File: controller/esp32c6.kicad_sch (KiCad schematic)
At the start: 13 parts, among them J10 Conn_ARM_JTAG_SWD_10, SW1 Boot, SW2 Reset, U6 ESP32-C6-WROOM-1

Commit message: Controller - some more changes
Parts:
- added D23, D24, D25: CLMUD-FKC-CHJNPM569ABB845343, Library:LED_Cree-PLCC4_1.5x1.5mm, symbol Device:LED_ARGB
- added R49, R50, R57, R58, R59, R60, R64, R65, R66: ?, Resistor_SMD:R_0402_1005Metric, symbol Device:R_Small
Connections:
- net +3V3: now also D23.1 (A), D24.1 (A), D25.1 (A)
- net RX: now also U6.24 (U0RXD/GPIO17); no longer U6.20 (GPIO22)
- net TX: now also U6.25 (U0TXD/GPIO16); no longer U6.21 (GPIO23)
- net IO10: now reaches U6.11 (GPIO10)
- net IO10: now also R49.1
- net IO11: now reaches U6.12 (GPIO11)
- net IO11: now also R50.1
- net IO18: now reaches U6.16 (GPIO18)
- net IO18: now also R58.1
- net IO19: now reaches U6.17 (GPIO19)
- net IO19: now also R59.1
- net IO15: now reaches U6.23 (GPIO15)
- net IO15: now also R57.1
- net IO3: now reaches U6.26 (GPIO3/ADC1_CH3)
- net IO3: now also R66.1
- net IO2: now reaches U6.27 (GPIO2/ADC1_CH2)
- net IO2: now also R65.1
- net IO0: now reaches U6.8 (GPIO0/ADC1_CH0/XTAL_32K_P)
- net IO0: now also R60.1
- net IO1: now reaches U6.9 (GPIO1/ADC1_CH1/XTAL_32K_N)
- net IO1: now also R64.1
- new net: D25.4 (BK), R66.2
- new net: D25.3 (GK), R65.2
- new net: D23.4 (BK), R57.2
- new net: D24.4 (BK), R60.2
- new net: D25.2 (RK), R64.2
- new net: D24.3 (GK), R59.2
- new net: D24.2 (RK), R58.2
- new net: D23.3 (GK), R50.2
- new net: D23.2 (RK), R49.2

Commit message: Controller - more changes
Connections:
- net B_BOOT: now reaches R7.2, SW1.1, U6.15 (GPIO9)
- net R: now reaches R10.2, U6.10 (GPIO8)
- net G: now reaches U6.20 (GPIO22)
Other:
- moved on the sheet: R10, R7, SW1
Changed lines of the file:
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@@
 	)
 	(junction
+		(at 92.71 88.9)
+		(diameter 0)
+		(color 0 0 0 0)
+	)
+	(junction
 		(at 146.05 60.96)
 		(diameter 0)
@@
 	)
 	(junction
+		(at 95.25 93.98)
+		(diameter 0)
+		(color 0 0 0 0)
+	)
+	(junction
+		(at 90.17 96.52)
+		(diameter 0)
+		(color 0 0 0 0)
+	)
+	(junction
 		(at 151.13 60.96)
 		(diameter 0)
@@
 		(color 0 0 0 0)
 	)
-	(junction
-		(at 93.98 88.9)
-		(diameter 0)
-		(color 0 0 0 0)
+	(wire
+		(pts
+			(xy 80.01 93.98) (xy 80.01 95.25)
+		)
+		(stroke
+			(width 0)
+			(type default)
+		)
 	)
 	(wire
@@
 	(wire
 		(pts
+			(xy 91.44 96.52) (xy 91.44 100.33)
+		)
+		(stroke
+			(width 0)
+			(type default)
+		)
+	)
+	(wire
+		(pts
 			(xy 170.18 93.98) (xy 171.45 93.98)
 		)
@@
 	(wire
 		(pts
+			(xy 90.17 96.52) (xy 91.44 96.52)
+		)
+		(stroke
+			(width 0)
+			(type default)
+		)
+	)
+	(wire
+		(pts
 			(xy 87.63 81.28) (xy 100.33 81.28)
 		)
@@
 	(wire
 		(pts
-			(xy 156.21 101.6) (xy 162.56 101.6)
+			(xy 95.25 93.98) (xy 100.33 93.98)
 		)
 		(stroke
@@
 	(wire
 		(pts
-			(xy 171.45 66.04) (xy 171.45 67.31)
+			(xy 156.21 101.6) (xy 162.56 101.6)
 		)
 		(stroke
@@
 	(wire
 		(pts
-			(xy 93.98 88.9) (xy 96.52 88.9)
+			(xy 171.45 66.04) (xy 171.45 67.31)
 		)
 		(stroke
@@
 	(wire
 		(pts
+			(xy 92.71 88.9) (xy 90.17 88.9)
+		)
+		(stroke
+			(width 0)
+			(type default)
+		)
+	)
+	(wire
+		(pts
 			(xy 90.17 111.76) (xy 100.33 111.76)
 		)
@@
 	(wire
 		(pts
-			(xy 93.98 88.9) (xy 91.44 88.9)
+			(xy 92.71 88.9) (xy 95.25 88.9)
+		)
+		(stroke
+			(width 0)
+			(type default)
+		)
+	)
+	(wire
+		(pts
+			(xy 77.47 93.98) (xy 80.01 93.98)
 		)
 		(stroke
@@
 	(wire
 		(pts
-			(xy 90.17 96.52) (xy 91.44 96.52)
+			(xy 90.17 100.33) (xy 91.44 100.33)
 		)
 		(stroke
@@
 	(wire
 		(pts
-			(xy 96.52 93.98) (xy 100.33 93.98)
-		)
-		(stroke
-			(width 0)
-			(type default)
-		)
-	)
-	(wire
-		(pts
 			(xy 151.13 60.96) (xy 156.21 60.96)
 		)
@@
 	(wire
 		(pts
-			(xy 91.44 93.98) (xy 91.44 96.52)
+			(xy 90.17 93.98) (xy 90.17 96.52)
 		)
 		(stroke
@@
 	(wire
 		(pts
+			(xy 93.98 95.25) (xy 93.98 93.98)
+		)
+		(stroke
+			(width 0)
+			(type default)
+		)
+	)
+	(wire
+		(pts
 			(xy 156.21 96.52) (xy 160.02 96.52)
 		)
@@
 	(wire
 		(pts
-			(xy 80.01 96.52) (xy 80.01 101.6)
+			(xy 80.01 100.33) (xy 80.01 105.41)
+		)
+		(stroke
+			(width 0)
+			(type default)
+		)
+	)
+	(wire
+		(pts
+			(xy 93.98 93.98) (xy 95.25 93.98)
+		)
+		(stroke
+			(width 0)
+			(type default)
+		)
+	)
+	(wire
+		(pts
+			(xy 77.47 96.52) (xy 90.17 96.52)
 		)
 		(stroke
@@
 		)
 	)
+	(wire
+		(pts
+			(xy 80.01 95.25) (xy 93.98 95.25)
+		)
+		(stroke
+			(width 0)
+			(type default)
+		)
+	)
 	(label "IO19"
 		(at 133.35 43.18 270)
@@
 		)
 	)
+	(hierarchical_label "B_BOOT"
+		(shape bidirectional)
+		(at 77.47 96.52 180)
+		(fields_autoplaced yes)
+		(effects
+			(font
+				(size 1.27 1.27)
+			)
+			(justify right)
+		)
+	)
 	(hierarchical_label "USB_D+"
 		(shape bidirectional)
@@
 		)
 	)
+	(hierarchical_label "G"
+		(shape input)
+		(at 100.33 116.84 180)
+		(fields_autoplaced yes)
+		(effects
+			(font
+				(size 1.27 1.27)
+			)
+			(justify right)
+		)
+	)
 	(hierarchical_label "GPIO20"
 		(shape bidirectional)
@@
 		)
 	)
+	(hierarchical_label "R"
+		(shape output)
+		(at 77.47 93.98 180)
+		(fields_autoplaced yes)
+		(effects
+			(font
+				(size 1.27 1.27)
+			)
+			(justify right)
+		)
+	)
 	(hierarchical_label "USB_D-"
 		(shape bidirectional)
@@
 	(symbol
 		(lib_id "Device:R_Small")
-		(at 91.44 91.44 0)
+		(at 90.17 91.44 0)
 		(unit 1)
 		(exclude_from_sim no)
@@
 		(dnp no)
 		(property "Reference" "R7"
-			(at 89.408 98.044 0)
+			(at 88.138 98.044 0)
 			(effects
 				(font
@@
 		)
 		(property "Value" "10k"
-			(at 91.44 93.218 90)
+			(at 90.17 93.218 90)
 			(effects
 				(font
@@
 		)
 		(property "Footprint" "Resistor_SMD:R_0603_1608Metric"
-			(at 91.44 91.44 0)
+			(at 90.17 91.44 0)
 			(effects
 				(font
@@
 		)
 		(property "Datasheet" "~"
-			(at 91.44 91.44 0)
+			(at 90.17 91.44 0)
 			(effects
 				(font
@@
 		)
 		(property "Description" "Resistor, small symbol"
-			(at 91.44 91.44 0)
+			(at 90.17 91.44 0)
 			(effects
 				(font
@@
 	(symbol
 		(lib_id "power:Earth")
-		(at 80.01 101.6 0)
+		(at 80.01 105.41 0)
 		(mirror y)
 		(unit 1)
@@
 		(fields_autoplaced yes)
 		(property "Reference" "#PWR043"
-			(at 80.01 107.95 0)
+			(at 80.01 111.76 0)
 			(effects
 				(font
@@
 		)
 		(property "Value" "Earth"
-			(at 80.01 106.68 0)
+			(at 80.01 110.49 0)
 			(effects
 				(font
@@
 		)
 		(property "Footprint" ""
-			(at 80.01 101.6 0)
+			(at 80.01 105.41 0)
 			(effects
 				(font
@@
 		)
 		(property "Datasheet" "~"
-			(at 80.01 101.6 0)
+			(at 80.01 105.41 0)
 			(effects
 				(font
@@
 		)
 		(property "Description" "Power symbol creates a global label with name \"Earth\""
-			(at 80.01 101.6 0)
+			(at 80.01 105.41 0)
 			(effects
 				(font
@@
 	(symbol
 		(lib_id "power:+3V3")
-		(at 93.98 88.9 0)
+		(at 92.71 88.9 0)
 		(unit 1)
 		(exclude_from_sim no)
@@
 		(fields_autoplaced yes)
 		(property "Reference" "#PWR044"
-			(at 93.98 92.71 0)
+			(at 92.71 92.71 0)
 			(effects
 				(font
@@
 		)
 		(property "Value" "+3V3"
-			(at 93.98 85.09 0)
+			(at 92.71 85.09 0)
 			(effects
 				(font
@@
 		)
 		(property "Footprint" ""
-			(at 93.98 88.9 0)
+			(at 92.71 88.9 0)
 			(effects
 				(font
@@
 		)
 		(property "Datasheet" ""
-			(at 93.98 88.9 0)
+			(at 92.71 88.9 0)
 			(effects
 				(font
@@
 		)
 		(property "Description" "Power symbol creates a global label with name \"+3V3\""
-			(at 93.98 88.9 0)
+			(at 92.71 88.9 0)
 			(effects
 				(font
@@
 	(symbol
 		(lib_id "Device:R_Small")
-		(at 96.52 91.44 0)
+		(at 95.25 91.44 0)
 		(unit 1)
 		(exclude_from_sim no)
@@
 		(dnp no)
 		(property "Reference" "R10"
-			(at 94.742 95.25 0)
+			(at 96.266 90.17 0)
 			(effects
 				(font
@@
 		)
 		(property "Value" "10k"
-			(at 96.52 93.218 90)
+			(at 95.25 93.218 90)
 			(effects
 				(font
@@
 		)
 		(property "Footprint" "Resistor_SMD:R_0603_1608Metric"
-			(at 96.52 91.44 0)
+			(at 95.25 91.44 0)
 			(effects
 				(font
@@
 		)
 		(property "Datasheet" "~"
-			(at 96.52 91.44 0)
+			(at 95.25 91.44 0)
 			(effects
 				(font
@@
 		)
 		(property "Description" "Resistor, small symbol"
-			(at 96.52 91.44 0)
+			(at 95.25 91.44 0)
 			(effects
 				(font
@@
 	(symbol
 		(lib_id "Switch:SW_Push")
-		(at 85.09 96.52 0)
+		(at 85.09 100.33 0)
 		(mirror y)
 		(unit 1)
@@
 		(on_board yes)
 		(dnp no)
-		(fields_autoplaced yes)
 		(property "Reference" "SW1"
-			(at 85.09 88.9 0)
+			(at 85.09 101.854 0)
 			(effects
 				(font
@@
 		)
 		(property "Value" "Boot"
-			(at 85.09 91.44 0)
+			(at 85.09 104.394 0)
 			(effects
 				(font
@@
 		)
 		(property "Footprint" ""
-			(at 85.09 91.44 0)
+			(at 85.09 95.25 0)
 			(effects
 				(font
@@
 		)
 		(property "Datasheet" "~"
-			(at 85.09 91.44 0)
+			(at 85.09 95.25 0)
 			(effects
 				(font
@@
 		)
 		(property "Description" "Push button switch, generic, two pins"
-			(at 85.09 96.52 0)
+			(at 85.09 100.33 0)
 			(effects
 				(font

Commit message: Controller - Even more pins
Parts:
- J10: footprint (none) -> Connector_PinHeader_1.27mm:PinHeader_2x05_P1.27mm_Vertical_SMD
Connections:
- net +3V3: now also J10.1 (VTref)
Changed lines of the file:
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@@
+	)
+	(symbol
+		(lib_id "power:+3V3")
+		(at 184.15 86.36 0)
+		(unit 1)
+		(exclude_from_sim no)
+		(in_bom yes)
+		(on_board yes)
+		(dnp no)
+		(fields_autoplaced yes)
+		(property "Reference" "#PWR0143"
+			(at 184.15 90.17 0)
+			(effects
+				(font
+					(size 1.27 1.27)
+				)
+				(hide yes)
+			)
+		)
+		(property "Value" "+3V3"
+			(at 184.15 82.55 0)
+			(effects
+				(font
+					(size 1.27 1.27)
+				)
+			)
+		)
+		(property "Footprint" ""
+			(at 184.15 86.36 0)
+			(effects
+				(font
+					(size 1.27 1.27)
+				)
+				(hide yes)
+			)
+		)
+		(property "Datasheet" ""
+			(at 184.15 86.36 0)
+			(effects
+				(font
+					(size 1.27 1.27)
+				)
+				(hide yes)
+			)
+		)
+		(property "Description" "Power symbol creates a global label with name \"+3V3\""
+			(at 184.15 86.36 0)
+			(effects
+				(font
+					(size 1.27 1.27)
+				)
+				(hide yes)
+			)
+		)
+		(pin "1"
+		)
+		(instances
+			(project "controller"
+				(path "/5b092a03-7e3e-4df1-ad91-2ac0e362f857/d740d1c6-5e66-443f-883c-6d6068be0c77"
+					(reference "#PWR0143")
+					(unit 1)
+				)
+			)
+		)
 	)
 	(symbol
@@
 			)
 		)
-		(property "Footprint" ""
+		(property "Footprint" "Connector_PinHeader_1.27mm:PinHeader_2x05_P1.27mm_Vertical_SMD"
 			(at 184.15 101.6 0)
 			(effects

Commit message: Add new leds
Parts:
- removed D23, D24, D25: CLMUD-FKC-CHJNPM569ABB845343, Library:LED_Cree-PLCC4_1.5x1.5mm, symbol Device:LED_ARGB
- removed R49, R50, R57, R58, R59, R60, R64, R65, R66: ?, Resistor_SMD:R_0402_1005Metric, symbol Device:R_Small
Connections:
- net G renamed LED_CH2
- net IO0: no longer names the net of U6.8 (GPIO0/ADC1_CH0/XTAL_32K_P)
- net IO1: no longer names the net of U6.9 (GPIO1/ADC1_CH1/XTAL_32K_N)
- net IO10: no longer names the net of U6.11 (GPIO10)
- net IO11: no longer names the net of U6.12 (GPIO11)
- net IO15: no longer names the net of U6.23 (GPIO15)
- net IO18: no longer names the net of U6.16 (GPIO18)
- net IO19: no longer names the net of U6.17 (GPIO19)
- net IO2: no longer names the net of U6.27 (GPIO2/ADC1_CH2)
- net IO3: no longer names the net of U6.26 (GPIO3/ADC1_CH3)
- net R renamed LED_CH1

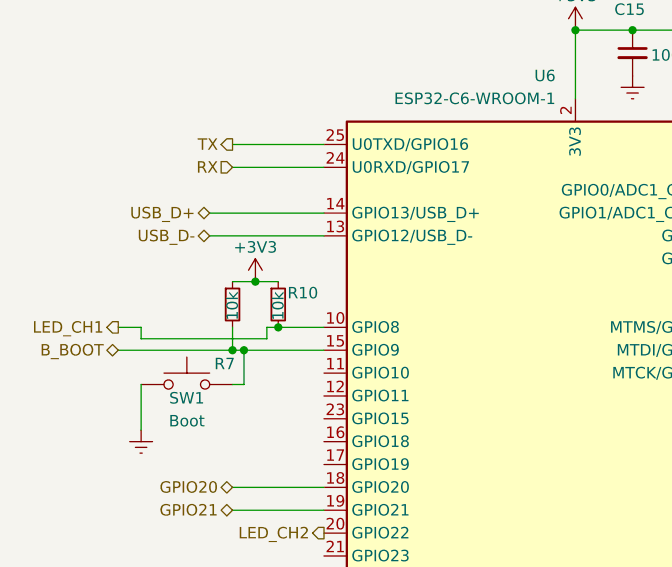
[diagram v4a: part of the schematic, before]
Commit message: Controller - Most things routed
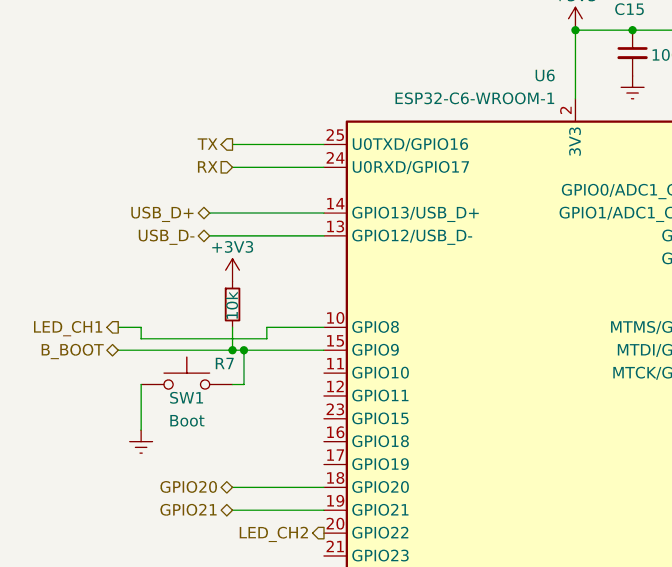
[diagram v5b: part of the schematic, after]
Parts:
- removed R10: 10k, Resistor_SMD:R_0603_1608Metric, symbol Device:R_Small
- R11: footprint Resistor_SMD:R_0603_1608Metric -> Resistor_SMD:R_0402_1005Metric
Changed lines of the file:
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@@
-	)
-	(junction
-		(at 92.71 88.9)
-		(diameter 0)
-		(color 0 0 0 0)
 	)
 	(junction
@@
 	)
 	(junction
-		(at 95.25 93.98)
-		(diameter 0)
-		(color 0 0 0 0)
-	)
-	(junction
 		(at 90.17 96.52)
 		(diameter 0)
@@
 	(wire
 		(pts
-			(xy 95.25 93.98) (xy 100.33 93.98)
+			(xy 93.98 93.98) (xy 100.33 93.98)
 		)
 		(stroke
@@
 	(wire
 		(pts
-			(xy 92.71 88.9) (xy 90.17 88.9)
-		)
-		(stroke
-			(width 0)
-			(type default)
-		)
-	)
-	(wire
-		(pts
 			(xy 90.17 111.76) (xy 100.33 111.76)
 		)
@@
 	(wire
 		(pts
-			(xy 92.71 88.9) (xy 95.25 88.9)
-		)
-		(stroke
-			(width 0)
-			(type default)
-		)
-	)
-	(wire
-		(pts
 			(xy 77.47 93.98) (xy 80.01 93.98)
 		)
@@
 		(pts
 			(xy 80.01 100.33) (xy 80.01 105.41)
-		)
-		(stroke
-			(width 0)
-			(type default)
-		)
-	)
-	(wire
-		(pts
-			(xy 93.98 93.98) (xy 95.25 93.98)
 		)
 		(stroke
@@
 	(symbol
 		(lib_id "power:+3V3")
-		(at 92.71 88.9 0)
+		(at 90.17 88.9 0)
 		(unit 1)
 		(exclude_from_sim no)
@@
 		(fields_autoplaced yes)
 		(property "Reference" "#PWR044"
-			(at 92.71 92.71 0)
+			(at 90.17 92.71 0)
 			(effects
 				(font
@@
 		)
 		(property "Value" "+3V3"
-			(at 92.71 85.09 0)
+			(at 90.17 85.09 0)
 			(effects
 				(font
@@
 		)
 		(property "Footprint" ""
-			(at 92.71 88.9 0)
+			(at 90.17 88.9 0)
 			(effects
 				(font
@@
 		)
 		(property "Datasheet" ""
-			(at 92.71 88.9 0)
+			(at 90.17 88.9 0)
 			(effects
 				(font
@@
 		)
 		(property "Description" "Power symbol creates a global label with name \"+3V3\""
-			(at 92.71 88.9 0)
+			(at 90.17 88.9 0)
 			(effects
 				(font
@@
 	)
 	(symbol
-		(lib_id "Device:R_Small")
-		(at 95.25 91.44 0)
-		(unit 1)
-		(exclude_from_sim no)
-		(in_bom yes)
-		(on_board yes)
-		(dnp no)
-		(property "Reference" "R10"
-			(at 96.266 90.17 0)
-			(effects
-				(font
-					(size 1.27 1.27)
-				)
-				(justify left)
-			)
-		)
-		(property "Value" "10k"
-			(at 95.25 93.218 90)
-			(effects
-				(font
-					(size 1.27 1.27)
-				)
-				(justify left)
-			)
-		)
-		(property "Footprint" "Resistor_SMD:R_0603_1608Metric"
-			(at 95.25 91.44 0)
-			(effects
-				(font
-					(size 1.27 1.27)
-				)
-				(hide yes)
-			)
-		)
-		(property "Datasheet" "~"
-			(at 95.25 91.44 0)
-			(effects
-				(font
-					(size 1.27 1.27)
-				)
-				(hide yes)
-			)
-		)
-		(property "Description" "Resistor, small symbol"
-			(at 95.25 91.44 0)
-			(effects
-				(font
-					(size 1.27 1.27)
-				)
-				(hide yes)
-			)
-		)
-		(pin "1"
-		)
-		(pin "2"
-		)
-		(instances
-			(project "controller"
-				(path "/5b092a03-7e3e-4df1-ad91-2ac0e362f857/d740d1c6-5e66-443f-883c-6d6068be0c77"
-					(reference "R10")
-					(unit 1)
-				)
-			)
-		)
-	)
-	(symbol
 		(lib_id "power:Earth")
 		(at 146.05 66.04 0)
@@
 			)
 		)
-		(property "Footprint" "Resistor_SMD:R_0603_1608Metric"
+		(property "Footprint" "Resistor_SMD:R_0402_1005Metric"
 			(at 171.45 69.85 0)
 			(effects

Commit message: Controller - Fix all DRC errors and some warnings
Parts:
- SW1, SW2: footprint (none) -> Button_Switch_SMD:SW_SPST_B3U-1000P
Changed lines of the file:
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@@
 			)
 		)
-		(property "Footprint" ""
+		(property "Footprint" "Button_Switch_SMD:SW_SPST_B3U-1000P"
 			(at 193.04 68.58 0)
 			(effects
@@
 			)
 		)
-		(property "Footprint" ""
+		(property "Footprint" "Button_Switch_SMD:SW_SPST_B3U-1000P"
 			(at 85.09 95.25 0)
 			(effects

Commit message: controller - Update BOM - WIP
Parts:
- C15, C20: value 100nF -> 100nF 9V
- C16, C17, C18: value 10uF -> 10uF 9V
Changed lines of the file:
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@@
 			)
 		)
-		(property "Value" "10uF"
+		(property "Value" "10uF 9V"
 			(at 148.336 69.85 0)
 			(effects
@@
 		)
 		(property "Description" "Unpolarized capacitor, small symbol"
+			(at 151.13 63.5 0)
+			(effects
+				(font
+					(size 1.27 1.27)
+				)
+				(hide yes)
+			)
+		)
+		(property "MFR" ""
+			(at 151.13 63.5 0)
+			(effects
+				(font
+					(size 1.27 1.27)
+				)
+				(hide yes)
+			)
+		)
+		(property "part-num" ""
 			(at 151.13 63.5 0)
 			(effects
@@
 			)
 		)
+		(property "MFR" ""
+			(at 90.17 91.44 0)
+			(effects
+				(font
+					(size 1.27 1.27)
+				)
+				(hide yes)
+			)
+		)
+		(property "part-num" ""
+			(at 90.17 91.44 0)
+			(effects
+				(font
+					(size 1.27 1.27)
+				)
+				(hide yes)
+			)
+		)
 		(pin "1"
 		)
@@
 			)
 		)
-		(property "Value" "10uF"
+		(property "Value" "10uF 9V"
 			(at 153.67 69.85 0)
 			(effects
@@
 		)
 		(property "Description" "Unpolarized capacitor, small symbol"
+			(at 156.21 63.5 0)
+			(effects
+				(font
+					(size 1.27 1.27)
+				)
+				(hide yes)
+			)
+		)
+		(property "MFR" ""
+			(at 156.21 63.5 0)
+			(effects
+				(font
+					(size 1.27 1.27)
+				)
+				(hide yes)
+			)
+		)
+		(property "part-num" ""
 			(at 156.21 63.5 0)
 			(effects
@@
 			)
 		)
+		(property "MFR" ""
+			(at 128.27 101.6 0)
+			(effects
+				(font
+					(size 1.27 1.27)
+				)
+				(hide yes)
+			)
+		)
+		(property "part-num" ""
+			(at 128.27 101.6 0)
+			(effects
+				(font
+					(size 1.27 1.27)
+				)
+				(hide yes)
+			)
+		)
 		(pin "22"
 		)
@@
 			)
 		)
+		(property "MFR" ""
+			(at 182.88 73.66 0)
+			(effects
+				(font
+					(size 1.27 1.27)
+				)
+				(hide yes)
+			)
+		)
+		(property "part-num" ""
+			(at 182.88 73.66 0)
+			(effects
+				(font
+					(size 1.27 1.27)
+				)
+				(hide yes)
+			)
+		)
 		(pin "1"
 		)
@@
 			)
 		)
-		(property "Value" "10uF"
+		(property "Value" "10uF 9V"
 			(at 143.51 69.85 0)
 			(effects
@@
 		)
 		(property "Description" "Unpolarized capacitor, small symbol"
+			(at 146.05 63.5 0)
+			(effects
+				(font
+					(size 1.27 1.27)
+				)
+				(hide yes)
+			)
+		)
+		(property "MFR" ""
+			(at 146.05 63.5 0)
+			(effects
+				(font
+					(size 1.27 1.27)
+				)
+				(hide yes)
+			)
+		)
+		(property "part-num" ""
 			(at 146.05 63.5 0)
 			(effects
@@
 			)
 		)
+		(property "MFR" ""
+			(at 193.04 73.66 0)
+			(effects
+				(font
+					(size 1.27 1.27)
+				)
+				(hide yes)
+			)
+		)
+		(property "part-num" ""
+			(at 193.04 73.66 0)
+			(effects
+				(font
+					(size 1.27 1.27)
+				)
+				(hide yes)
+			)
+		)
 		(pin "2"
 		)
@@
 			)
 		)
-		(property "Value" "100nF"
+		(property "Value" "100nF 9V"
 			(at 136.652 63.754 0)
 			(effects
@@
 		)
 		(property "Description" "Unpolarized capacitor, small symbol"
+			(at 134.62 63.5 0)
+			(effects
+				(font
+					(size 1.27 1.27)
+				)
+				(hide yes)
+			)
+		)
+		(property "MFR" ""
+			(at 134.62 63.5 0)
+			(effects
+				(font
+					(size 1.27 1.27)
+				)
+				(hide yes)
+			)
+		)
+		(property "part-num" ""
 			(at 134.62 63.5 0)
 			(effects
@@
 			)
 		)
+		(property "MFR" ""
+			(at 184.15 101.6 0)
+			(effects
+				(font
+					(size 1.27 1.27)
+				)
+				(hide yes)
+			)
+		)
+		(property "part-num" ""
+			(at 184.15 101.6 0)
+			(effects
+				(font
+					(size 1.27 1.27)
+				)
+				(hide yes)
+			)
+		)
 		(pin "7"
 		)
@@
 			)
 		)
+		(property "MFR" ""
+			(at 171.45 69.85 0)
+			(effects
+				(font
+					(size 1.27 1.27)
+				)
+				(hide yes)
+			)
+		)
+		(property "part-num" ""
+			(at 171.45 69.85 0)
+			(effects
+				(font
+					(size 1.27 1.27)
+				)
+				(hide yes)
+			)
+		)
 		(pin "1"
 		)
@@
 			)
 		)
-		(property "Value" "100nF"
+		(property "Value" "100nF 9V"
 			(at 174.498 77.724 0)
 			(effects
@@
 		)
 		(property "Description" "Unpolarized capacitor, small symbol"
+			(at 171.45 76.2 0)
+			(effects
+				(font
+					(size 1.27 1.27)
+				)
+				(hide yes)
+			)
+		)
+		(property "MFR" ""
+			(at 171.45 76.2 0)
+			(effects
+				(font
+					(size 1.27 1.27)
+				)
+				(hide yes)
+			)
+		)
+		(property "part-num" ""
 			(at 171.45 76.2 0)
 			(effects
@@
 			(at 85.09 100.33 0)
 			(effects
+				(font
+					(size 1.27 1.27)
+				)
+				(hide yes)
+			)
+		)
+		(property "MFR" ""
+			(at 85.09 100.33 0)
+			(effects
+				(font
+					(size 1.27 1.27)
+				)
+				(hide yes)
+			)
+		)
+		(property "part-num" ""
+			(at 85.09 100.33 0)
+			(effects
